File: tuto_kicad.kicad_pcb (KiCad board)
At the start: 4 copper layers, 48 x 38 mm, 43 parts, among them J201 Conn_ST_STDC14, J301 USB_C_Receptacle_USB2.0_16P, U201 STM32G431KBT6, U202 ADXL343, U301 MIC5317-3.3YM5-TR, U302 USBLC6-2SC6, Y201 16MHz

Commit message: First rev by M. FIACK
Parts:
- added R208: 2K2, Resistor_SMD:R_0603_1608Metric, F.Cu at (233.5, 96.5)
- added R209: 2K2, Resistor_SMD:R_0603_1608Metric, F.Cu at (238.5, 90.0)
- renumbered PWR to D201, RED to D202, BLUE to D203, GPIO to J203, I2C2 to J204, UART1 to J205, INT1_ACC to TP202, INT2_ACC to TP203
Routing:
- net GND: track 45.3 -> 37.7 mm, vias 33 -> 27
- net +3.3V: track 19.7 -> 14.2 mm, vias 12 -> 10

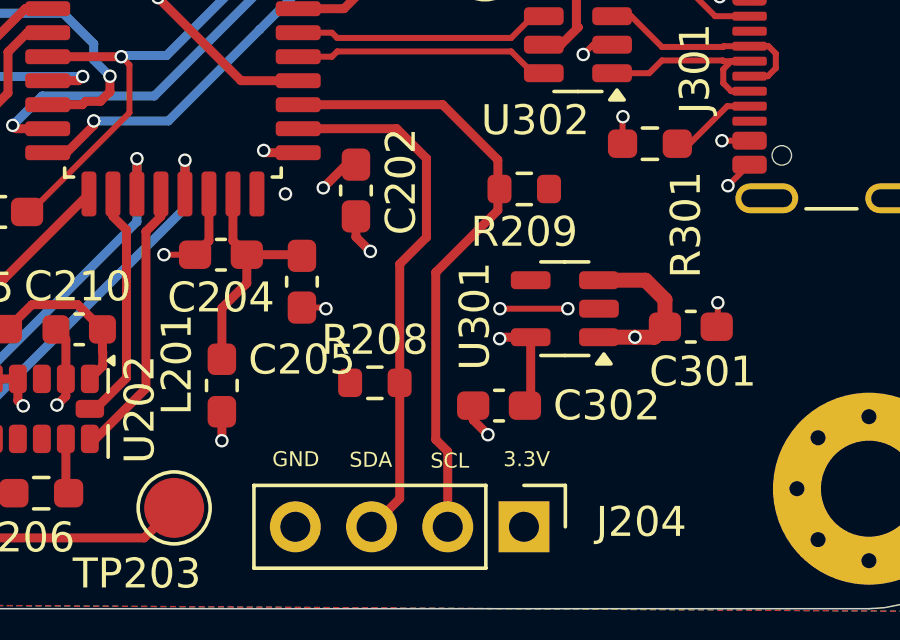
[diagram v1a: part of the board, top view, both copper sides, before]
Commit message: Pull-up resistors I2C added
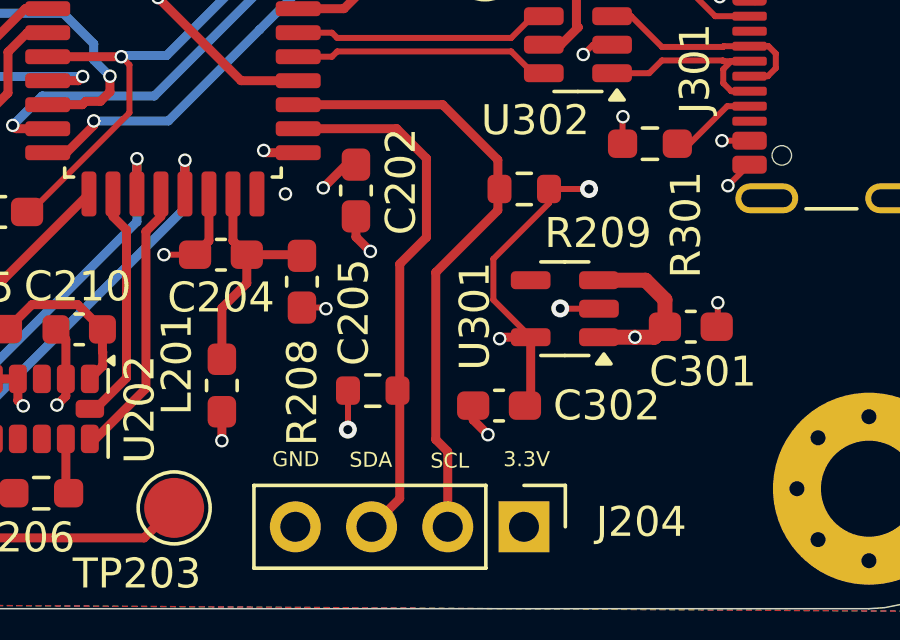
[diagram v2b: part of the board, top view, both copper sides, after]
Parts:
- moved R208 0.27 mm to (233.5, 96.7)
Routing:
- net +3.3V: track 14.2 -> 23.0 mm, vias 10 -> 12
- net GND: track 37.7 -> 36.7 mm, vias 27 -> 26
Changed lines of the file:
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@@
 		(tags "resistor")
 		(property "Reference" "R209"
-			(at 0 -1.43 0)
+			(at -2.46 -1.47 0)
 			(layer "F.SilkS")
 			(effects
@@
 	(footprint "Resistor_SMD:R_0603_1608Metric"
 		(layer "F.Cu")
-		(at 233.53 96.47)
+		(at 233.46 96.73)
 		(descr "Resistor SMD 0603 (1608 Metric), square (rectangular) end terminal, IPC-7351 nominal, (Body size source: IPC-SM-782 page 72, https://www.pcb-3d.com/wordpress/wp-content/uploads/ipc-sm-782a_amendment_1_and_2.pdf), generated with kicad-footprint-generator")
 		(tags "resistor")
 		(property "Reference" "R208"
-			(at 0 -1.43 0)
+			(at -2.35 0.06 90)
 			(layer "F.SilkS")
 			(effects
@@
 		(tags "capacitor handsolder")
 		(property "Reference" "C205"
-			(at 2.6 0 180)
+			(at 1.02 -1.73 270)
 			(layer "F.SilkS")
 			(effects
@@
 	)
 	(segment
+		(start 241 94)
+		(end 239.72 94)
+		(width 0.2)
+		(layer "F.Cu")
+		(net 1)
+	)
+	(segment
 		(start 243.215 75.725)
 		(end 243.225 75.735)
@@
 	)
 	(segment
-		(start 239.9625 94)
-		(end 237.7 94)
-		(width 0.2)
-		(layer "F.Cu")
-		(net 1)
-	)
-	(segment
 		(start 228 90.175)
 		(end 228 91.7375)
@@
 	)
 	(segment
+		(start 239.72 94)
+		(end 239.71 93.99)
+		(width 0.2)
+		(layer "F.Cu")
+		(net 1)
+	)
+	(segment
 		(start 218.65 86.1)
 		(end 218.65 85.7)
@@
 	)
 	(via
-		(at 239.9625 94)
-		(size 0.45)
-		(drill 0.3)
-		(layers "F.Cu" "B.Cu")
-		(remove_unused_layers yes)
-		(keep_end_layers yes)
-		(zone_layer_connections "In1.Cu")
-		(net 1)
-	)
-	(via
 		(at 215.85 85.25)
 		(size 0.45)
@@
 	)
 	(via
-		(at 245.3 89.9)
-		(size 0.45)
+		(at 239.71 93.99)
+		(size 0.6)
 		(drill 0.3)
 		(layers "F.Cu" "B.Cu")
-		(remove_unused_layers yes)
-		(keep_end_layers yes)
-		(zone_layer_connections "In1.Cu")
 		(net 1)
 	)
 	(via
-		(at 243.225 73.185)
+		(at 245.3 89.9)
 		(size 0.45)
 		(drill 0.3)
@@
 	)
 	(via
-		(at 237.7 94)
+		(at 243.225 73.185)
 		(size 0.45)
 		(drill 0.3)
@@
 	)
 	(segment
+		(start 239.335 90.01)
+		(end 240.67 90.01)
+		(width 0.2)
+		(layer "F.Cu")
+		(net 2)
+	)
+	(segment
+		(start 232.635 98.025)
+		(end 232.63 98.03)
+		(width 0.2)
+		(layer "F.Cu")
+		(net 2)
+	)
+	(segment
+		(start 239.335 90.01)
+		(end 239.335 90.485)
+		(width 0.2)
+		(layer "F.Cu")
+		(net 2)
+	)
+	(segment
 		(start 219.4575 93.8725)
 		(end 219.46 93.87)
@@
 	)
 	(segment
+		(start 239.335 90.485)
+		(end 237.48 92.34)
+		(width 0.2)
+		(layer "F.Cu")
+		(net 2)
+	)
+	(segment
 		(start 228.43 97.435)
 		(end 228.43 98.4)
@@
 	)
 	(segment
+		(start 237.48 92.34)
+		(end 237.48 93.705)
+		(width 0.2)
+		(layer "F.Cu")
+		(net 2)
+	)
+	(segment
 		(start 243.295 78.265)
 		(end 243.3 78.26)
@@
 	)
 	(segment
+		(start 232.635 96.73)
+		(end 232.635 98.025)
+		(width 0.2)
+		(layer "F.Cu")
+		(net 2)
+	)
+	(segment
 		(start 238.725 94.95)
 		(end 238.725 97.0375)
@@
 		(net 2)
 	)
+	(segment
+		(start 237.48 93.705)
+		(end 238.725 94.95)
+		(width 0.2)
+		(layer "F.Cu")
+		(net 2)
+	)
 	(via
 		(at 231.81 89.97)
@@
 		(net 2)
 	)
+	(via
+		(at 232.63 98.03)
+		(size 0.6)
+		(drill 0.3)
+		(layers "F.Cu" "B.Cu")
+		(net 2)
+	)
+	(via
+		(at 240.67 90.01)
+		(size 0.6)
+		(drill 0.3)
+		(layers "F.Cu" "B.Cu")
+		(net 2)
+	)

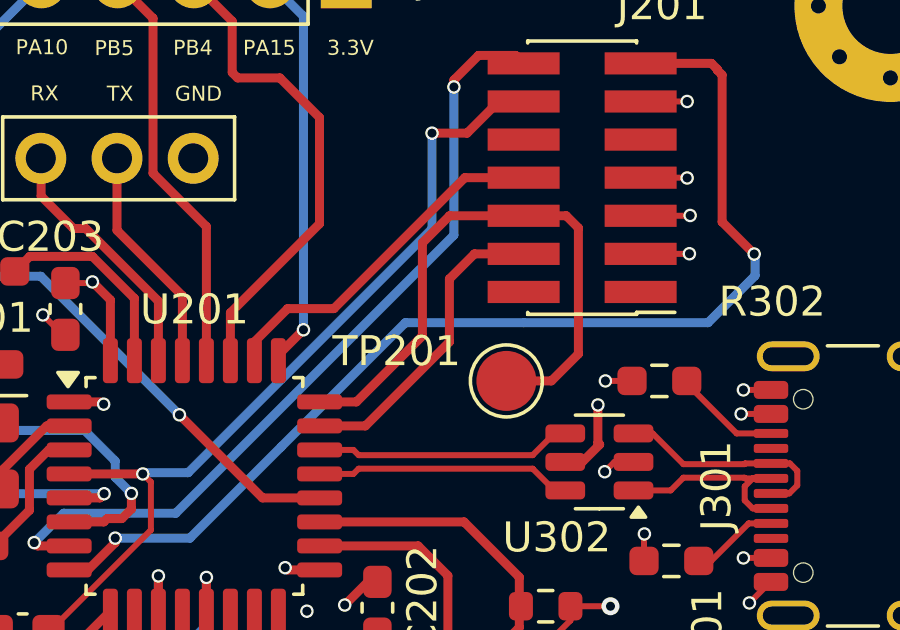
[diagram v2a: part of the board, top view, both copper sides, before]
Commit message: TestPoint in STLink connector deleted
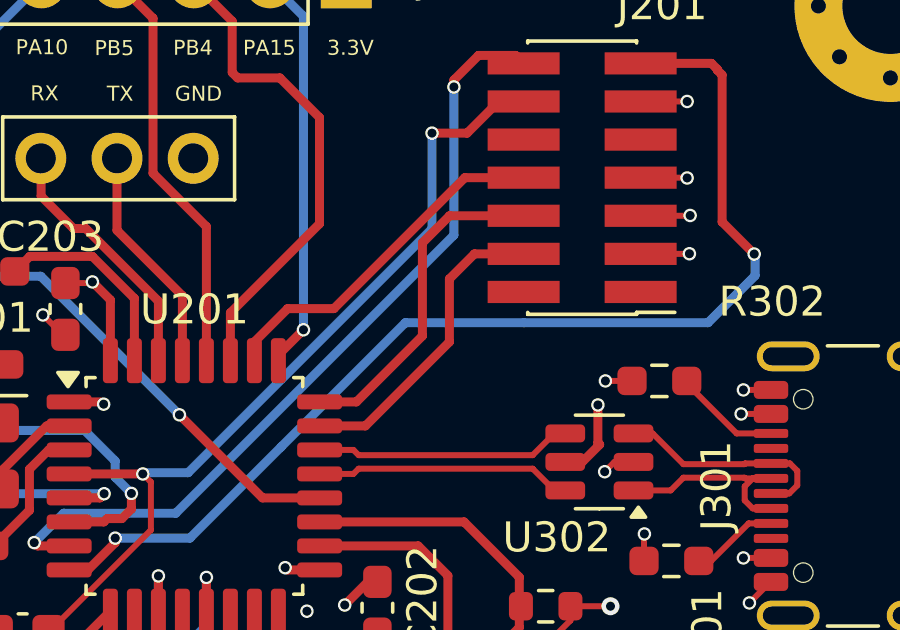
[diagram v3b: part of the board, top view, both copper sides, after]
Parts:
- removed TP201: TestPoint, TestPoint:TestPoint_Pad_D2.0mm
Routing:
- net SWCLK: track 20.2 -> 11.2 mm
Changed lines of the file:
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@@
 		)
 	)
-	(footprint "TestPoint:TestPoint_Pad_D2.0mm"
-		(layer "F.Cu")
-		(at 237.2 82.5)
-		(descr "SMD pad as test Point, diameter 2.0mm")
-		(tags "test point SMD pad")
-		(property "Reference" "TP201"
-			(at -3.66 -0.99 0)
-			(layer "F.SilkS")
-			(effects
-				(font
-					(size 1 1)
-					(thickness 0.15)
-				)
-			)
-		)
-		(property "Value" "TestPoint"
-			(at 0 2.05 0)
-			(layer "F.Fab")
-			(effects
-				(font
-					(size 1 1)
-					(thickness 0.15)
-				)
-			)
-		)
-		(property "Datasheet" "~"
-			(at 0 0 0)
-			(unlocked yes)
-			(layer "F.Fab")
-			(hide yes)
-			(effects
-				(font
-					(size 1.27 1.27)
-					(thickness 0.15)
-				)
-			)
-		)
-		(property "Description" "test point"
-			(at 0 0 0)
-			(unlocked yes)
-			(layer "F.Fab")
-			(hide yes)
-			(effects
-				(font
-					(size 1.27 1.27)
-					(thickness 0.15)
-				)
-			)
-		)
-		(property ki_fp_filters "Pin* Test*")
-		(sheetname "/STM32/")
-		(sheetfile "stm32.kicad_sch")
-		(attr exclude_from_pos_files)
-		(fp_circle
-			(center 0 0)
-			(end 0 1.2)
-			(stroke
-				(width 0.12)
-				(type solid)
-			)
-			(fill no)
-			(layer "F.SilkS")
-		)
-		(fp_circle
-			(center 0 0)
-			(end 1.5 0)
-			(stroke
-				(width 0.05)
-				(type solid)
-			)
-			(fill no)
-			(layer "F.CrtYd")
-		)
-		(fp_text user "${REFERENCE}"
-			(at 0 -2 0)
-			(layer "F.Fab")
-			(effects
-				(font
-					(size 1 1)
-					(thickness 0.15)
-				)
-			)
-		)
-		(pad "1" smd circle
-			(at 0 0)
-			(size 2 2)
-			(layers "F.Cu" "F.Mask")
-			(net 15 "SWCLK")
-			(pinfunction "1")
-			(pintype "passive")
-		)
-		(embedded_fonts no)
-	)
 	(footprint "Crystal:Crystal_SMD_EuroQuartz_MT-4Pin_3.2x2.5mm"
 		(layer "F.Cu")
@@
 	)
 	(segment
-		(start 239.195 76.995)
-		(end 239.6 77.4)
-		(width 0.3)
-		(layer "F.Cu")
-		(net 15)
-	)
-	(segment
-		(start 238.7 82.5)
-		(end 237.2 82.5)
-		(width 0.3)
-		(layer "F.Cu")
-		(net 15)
-	)
-	(segment
 		(start 232.2 83.2)
 		(end 234.4 81)
@@
 	)
 	(segment
-		(start 239.6 77.4)
-		(end 239.6 81.6)
-		(width 0.3)
-		(layer "F.Cu")
-		(net 15)
-	)
-	(segment
 		(start 235.305 76.995)
 		(end 237.775 76.995)
@@
 		(width 0.3)
 		(layer "F.Cu")
-		(net 15)
-	)
-	(segment
-		(start 237.775 76.995)
-		(end 239.195 76.995)
-		(width 0.3)
-		(layer "F.Cu")
-		(net 15)
-	)
-	(segment
-		(start 239.6 81.6)
-		(end 238.7 82.5)
-		(width 0.3)
-		(layer "F.Cu")

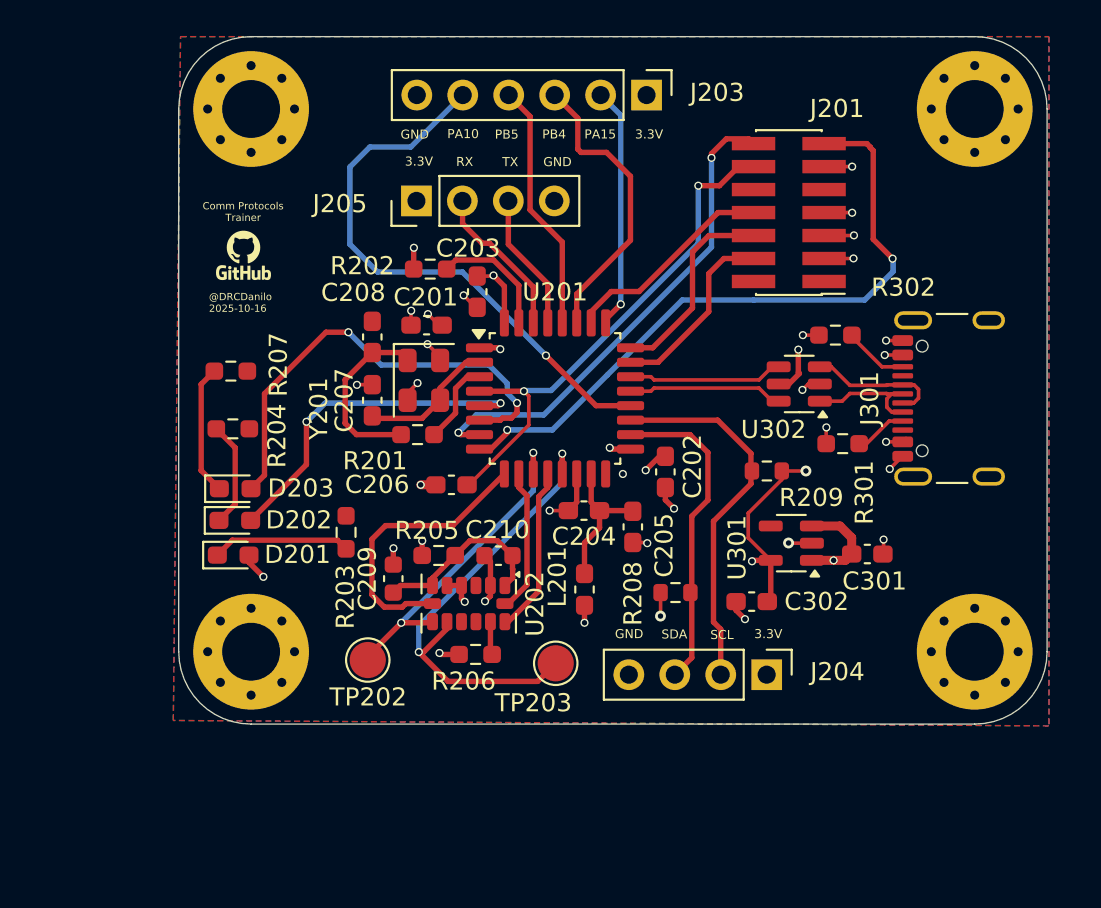
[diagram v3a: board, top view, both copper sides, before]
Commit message: SPI test points added
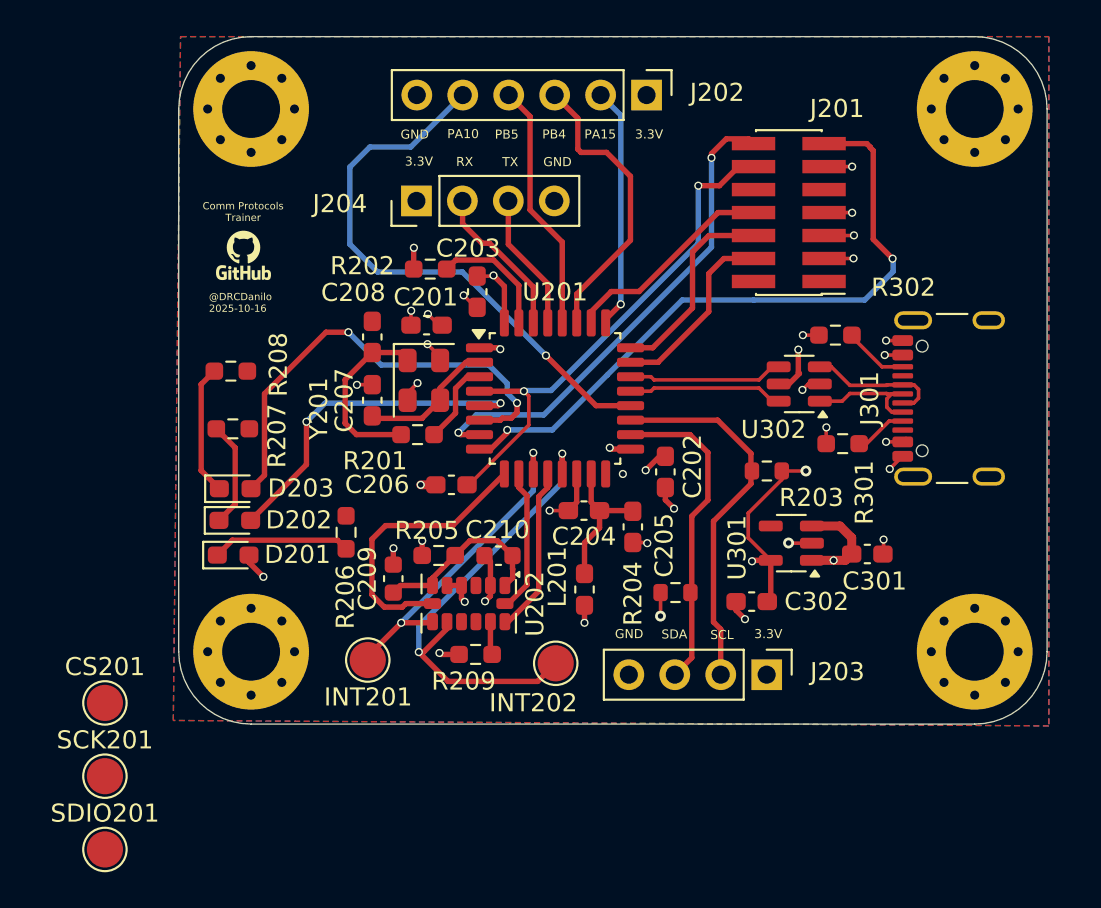
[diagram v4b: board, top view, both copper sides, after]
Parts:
- added CS201: CS, TestPoint:TestPoint_Pad_D2.0mm, F.Cu at (201.9, 102.8)
- added SCK201: SCK, TestPoint:TestPoint_Pad_D2.0mm, F.Cu at (201.9, 106.9)
- added SDIO201: SDIO, TestPoint:TestPoint_Pad_D2.0mm, F.Cu at (201.9, 110.9)
- INT201: renamed from TP202; value TestPoint -> INT1
- INT202: renamed from TP203; value TestPoint -> INT2
- renumbered J203 to J202, J204 to J203, J205 to J204, R209 to R203, R208 to R204, R203 to R206, R204 to R207, R207 to R208, R206 to R209

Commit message: SPI test points placed
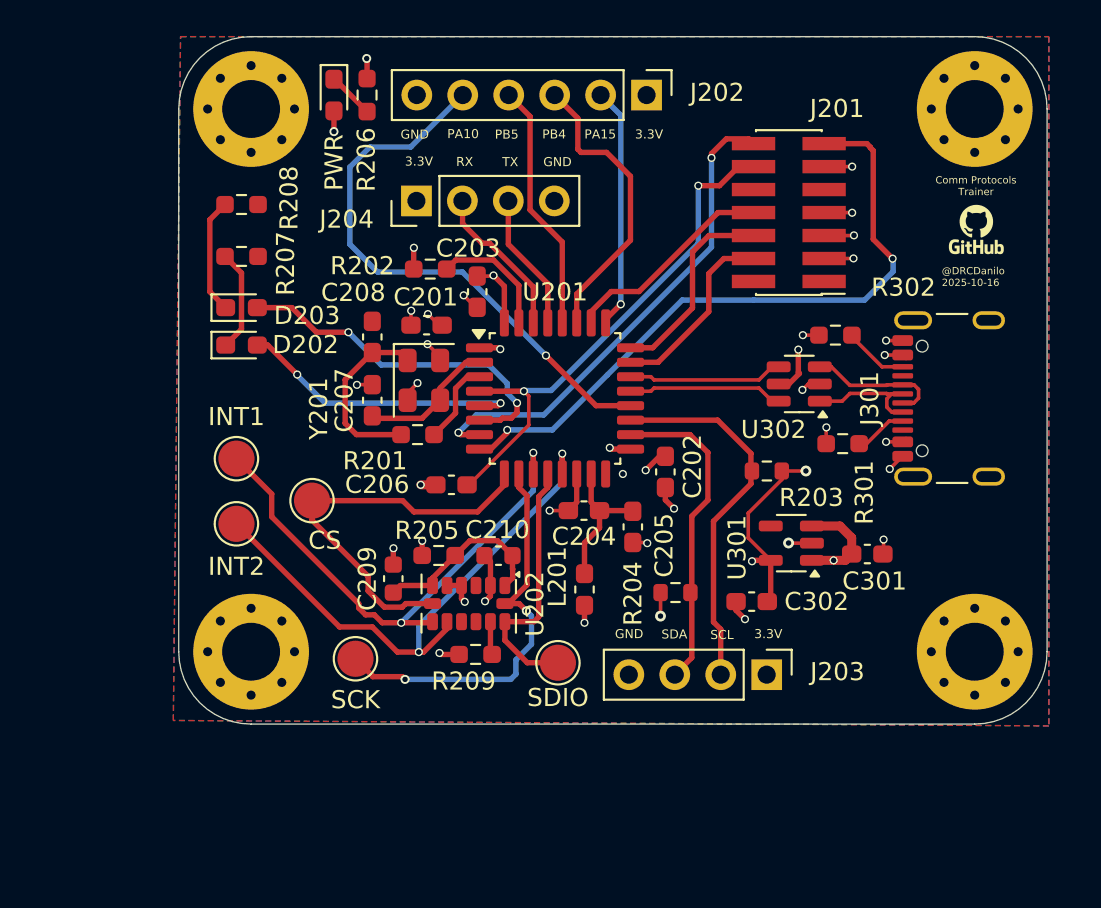
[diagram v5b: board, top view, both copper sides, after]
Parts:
- moved G*** 40.5 mm to (250.1, 76.7)
- moved SDIO 27.1 mm to (227.0, 100.6)
- moved PWR 26.0 mm to (214.6, 69.2), turned to -90 degrees
- moved R206 24.2 mm to (216.4, 69.2)
- moved INT2 19.3 mm to (209.2, 92.9)
- moved CS 16.0 mm to (213.4, 91.7)
- moved SCK 15.3 mm to (215.8, 100.4)
- moved INT1 13.3 mm to (209.2, 89.3)
- moved D203 10.0 mm to (209.5, 81.0)
- moved D202 9.70 mm to (209.5, 83.0)
- moved R207 9.54 mm to (209.5, 78.2)
- moved R208 9.23 mm to (209.5, 75.3)
- renumbered CS201 to CS, INT201 to INT1, INT202 to INT2, D201 to PWR, SCK201 to SCK, SDIO201 to SDIO
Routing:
- net SCK_ACCE_SPI1: track 7.97 -> 22.8 mm, vias 0 -> 2
- net INT1_ACCE: track 18.2 -> 29.1 mm
- net CS_ACCE_SP1: track 15.6 -> 22.4 mm
- net BLUE_LED: track 25.6 -> 19.6 mm
- net SDIO_ACCE_SPI1: track 9.26 -> 14.6 mm
- net Net-(D201-K): track 7.66 -> 2.57 mm
- net INT2_ACCE: track 26.5 -> 30.9 mm
- net RED_LED: track 19.1 -> 16.0 mm
- net GND: track 36.7 -> 37.8 mm, vias 26 -> 27
- net Net-(D203-K): track 7.22 -> 6.41 mm

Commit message: USB port placed at PCB edge
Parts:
- moved U302 1.61 mm to (241.9, 85.5)
- moved J301 0.63 mm to (250.3, 86.0)
- moved R302 0.61 mm to (242.7, 82.0)
- renumbered J203 to I2C2
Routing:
- net GND: track 37.8 -> 42.0 mm, vias 27 -> 29
- net +3.3V: track 22.7 -> 24.6 mm, vias 12 -> 13
- net /STM32/D-: track 8.56 -> 10.4 mm
- net /STM32/D+: track 8.56 -> 10.3 mm
- net /USB/CC2: track 3.58 -> 4.51 mm
- net /USB/USB_D-: track 7.21 -> 6.38 mm

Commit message: +5V pin added in I2C2 connector
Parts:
- I2C2: footprint Connector_PinHeader_2.54mm:PinHeader_1x04_P2.54mm_Vertical -> Connector_PinHeader_2.54mm:PinHeader_1x05_P2.54mm_Vertical
- moved I2C2 2.54 mm to (241.0, 101.3)
- renumbered CS to CS201, PWR to D201, INT1 to INT201, INT2 to INT202, SCK to SCK201, SDIO to SDIO201
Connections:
- I2C2 pad 1: +3.3V -> +5V
- I2C2 pad 2: I2C2_SCL -> +3.3V
- I2C2 pad 3: I2C2_SDA -> I2C2_SCL
- I2C2 pad 4: GND -> I2C2_SDA
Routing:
- net +5V: track 11.1 -> 13.6 mm, vias 4 -> 5

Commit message: Silkscreen layers finished
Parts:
- removed G***: LOGO, logoGitHub:logoGitHub
- renumbered J204 to USART1
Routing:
- net GND: track 42.0 -> 43.4 mm, vias 29 -> 115
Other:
- board text added: "2025-11-19"
- board text added: "3V3 RX TX GND"
- board text added: "@DRCDanilo"
- board text added: "BLUE"
- board text added: "CS"
- board text added: "Danilo Del Rio Cisneros"
- board text added: "GNDSDASCL3V35V"
- board text added: "GPIO"
- board text added: "INT1"
- board text added: "INT2"
- board text added: "PWR"
- board text added: "RED"
- board text added: "SCK"
- board text added: "SDIO"
- board text added: "github.com/DRCDanilo/CommTrainer_PCB"
- board text removed: "3.3V"
- board text removed: "@DRCDanilo 2025-10-16"
- board text removed: "GND"
- board text removed: "PA10"
- board text removed: "PA15"
- board text removed: "PB4"
- board text removed: "PB5"
- board text removed: "RX"
- board text removed: "SCL"
- board text removed: "SDA"
- board text removed: "TX"
